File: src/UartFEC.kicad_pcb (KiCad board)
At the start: 2 copper layers, 24 x 27.9 mm, 16 parts, among them J1 B3B-XH-A, P1 105444-0001, U1 FT232RL

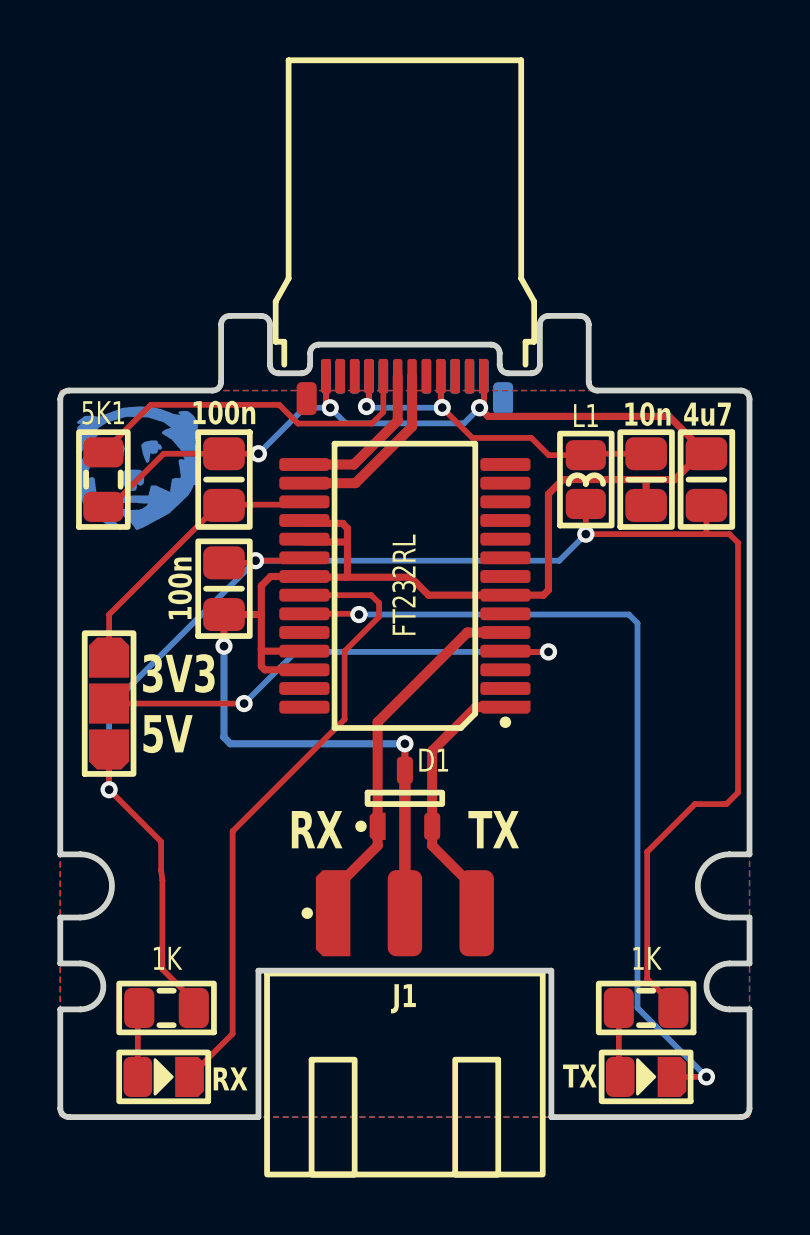
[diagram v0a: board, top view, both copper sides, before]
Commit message: Fixed reset pin (was GND before; now flloating)
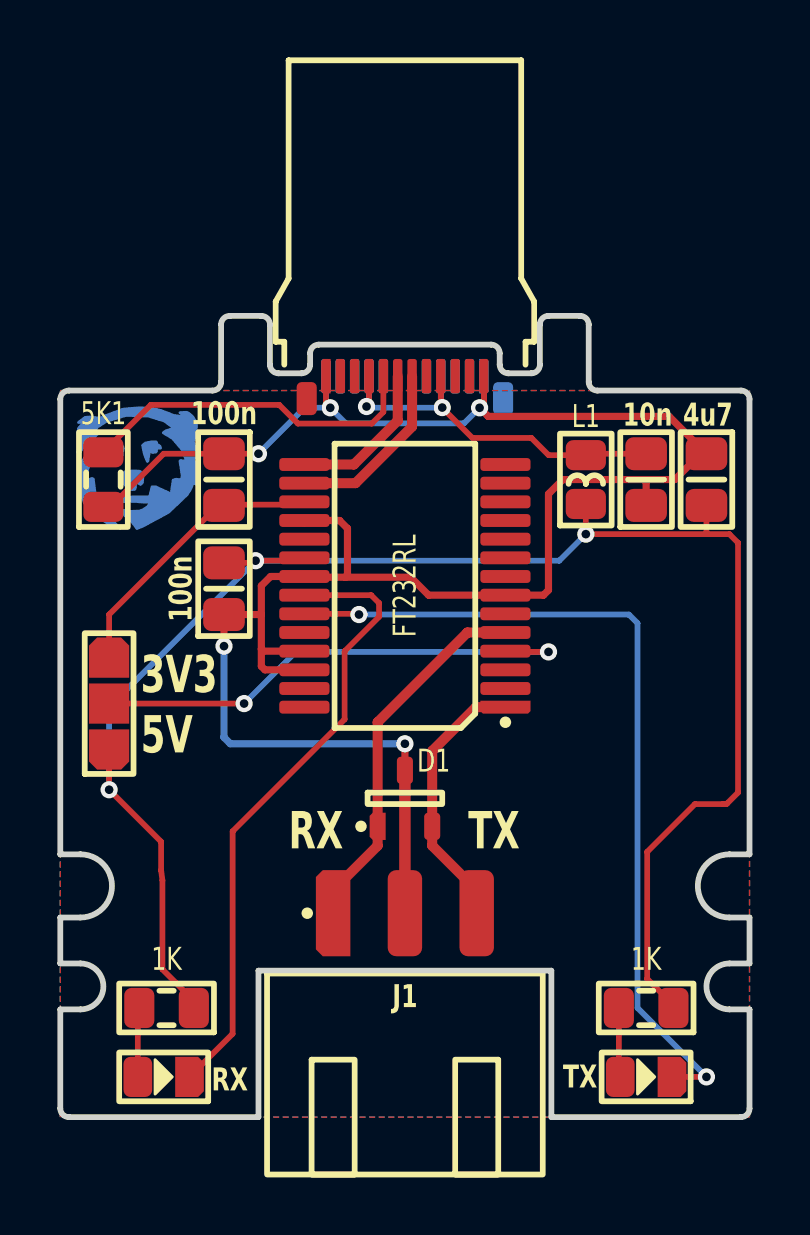
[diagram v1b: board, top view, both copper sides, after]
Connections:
- U1 pad 19: GND -> (no net)
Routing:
- net GND: track 78.3 -> 76.9 mm
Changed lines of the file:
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@@
       (net 7 "GND") (thermal_bridge_angle 45))
     (pad "19" smd roundrect locked (at 3.5 1.625 180) (size 1.75 0.45) (layers "F.Cu" "F.Paste" "F.Mask") (roundrect_rratio 0.25)
-      (net 7 "GND") (thermal_bridge_angle 45))
+      (thermal_bridge_angle 45))
     (pad "20" smd roundrect locked (at 3.5 0.975 180) (size 1.75 0.45) (layers "F.Cu" "F.Paste" "F.Mask") (roundrect_rratio 0.25)
       (net 3 "5V") (thermal_bridge_angle 45))
@@
   (segment (start 41.4 25.7) (end 42.3 24.8) (width 0.25) (layer "F.Cu") (net 7))
   (segment (start 36.825 29.725) (end 32.825 29.725) (width 0.25) (layer "F.Cu") (net 7))
-  (segment (start 29.825 27.225) (end 30 27.4) (width 0.25) (layer "F.Cu") (net 7))
   (segment (start 28.525 29.1) (end 29.925 29.1) (width 0.25) (layer "F.Cu") (net 7))
-  (segment (start 29.925 29.1) (end 30 29.025) (width 0.25) (layer "F.Cu") (net 7))
-  (segment (start 30 27.875) (end 28.5 27.875) (width 0.25) (layer "F.Cu") (net 7))
   (segment (start 25.7 30.4) (end 27 30.4) (width 0.25) (layer "F.Cu") (net 7))
-  (segment (start 30 27.4) (end 30 27.875) (width 0.25) (layer "F.Cu") (net 7))
   (segment (start 26.9 24.8) (end 25.7 24.8) (width 0.2) (layer "F.Cu") (net 7))
-  (segment (start 30 29.025) (end 30 27.875) (width 0.25) (layer "F.Cu") (net 7))
-  (segment (start 28.5 27.225) (end 29.825 27.225) (width 0.25) (layer "F.Cu") (net 7))
   (segment (start 37 29.55) (end 36.825 29.725) (width 0.25) (layer "F.Cu") (net 7))
+  (segment (start 30 27.4) (end 30 29.025) (width 0.25) (layer "F.Cu") (net 7))
   (segment (start 32 40.8) (end 32 35.825) (width 0.4) (layer "F.Cu") (net 7))
   (segment (start 40.325 25.7) (end 41.4 25.7) (width 0.25) (layer "F.Cu") (net 7))
@@
   (segment (start 28.5 31.675) (end 27.075 31.675) (width 0.25) (layer "F.Cu") (net 7))
   (segment (start 41.2 23.5) (end 42.5 24.8) (width 0.25) (layer "F.Cu") (net 7))
+  (segment (start 28.5 27.225) (end 28.6 27.125) (width 0.25) (layer "F.Cu") (net 7))
   (segment (start 32.825 29.725) (end 32.2 29.1) (width 0.25) (layer "F.Cu") (net 7))
   (segment (start 40.325 25.7) (end 40.4 25.775) (width 0.25) (layer "F.Cu") (net 7))
@@
   (segment (start 29.25 23.05) (end 29.4 23.2) (width 0.2) (layer "F.Cu") (net 7))
   (segment (start 40.325 25.7) (end 37.5 25.7) (width 0.25) (layer "F.Cu") (net 7))
+  (segment (start 30 29.025) (end 29.925 29.1) (width 0.25) (layer "F.Cu") (net 7))
   (segment (start 37 26.2) (end 37 29.55) (width 0.25) (layer "F.Cu") (net 7))
+  (segment (start 29.725 27.125) (end 30 27.4) (width 0.25) (layer "F.Cu") (net 7))
   (segment (start 34.75 23.05) (end 34.6 23.2) (width 0.2) (layer "F.Cu") (net 7))
   (segment (start 23.6 24.8) (end 25.7 24.8) (width 0.2) (layer "F.Cu") (net 7))
@@
   (segment (start 27 30.4) (end 27 31.6) (width 0.25) (layer "F.Cu") (net 7))
   (segment (start 37.5 25.7) (end 37 26.2) (width 0.25) (layer "F.Cu") (net 7))
+  (segment (start 28.6 27.125) (end 29.725 27.125) (width 0.25) (layer "F.Cu") (net 7))
   (segment (start 21.75 26.65) (end 23.6 24.8) (width 0.2) (layer "F.Cu") (net 7))
   (segment (start 32 35.825) (end 32 34.9) (width 0.25) (layer "F.Cu") (net 7))

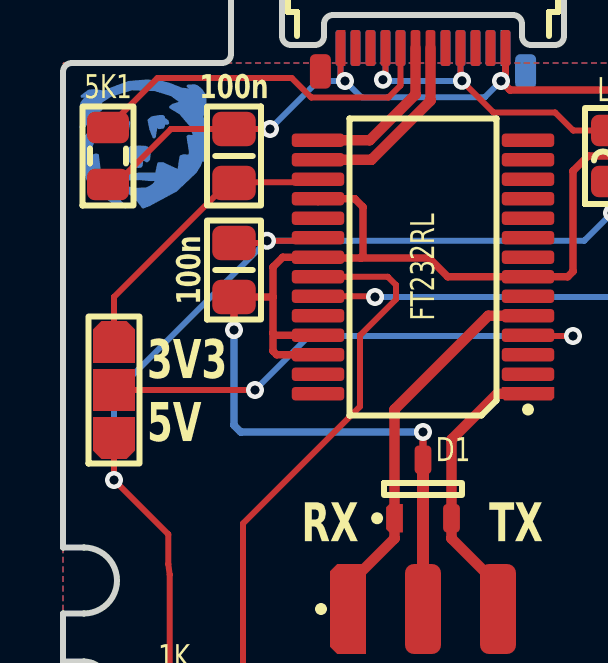
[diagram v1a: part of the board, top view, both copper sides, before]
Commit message: Updated jumper and JST edge connector footprint
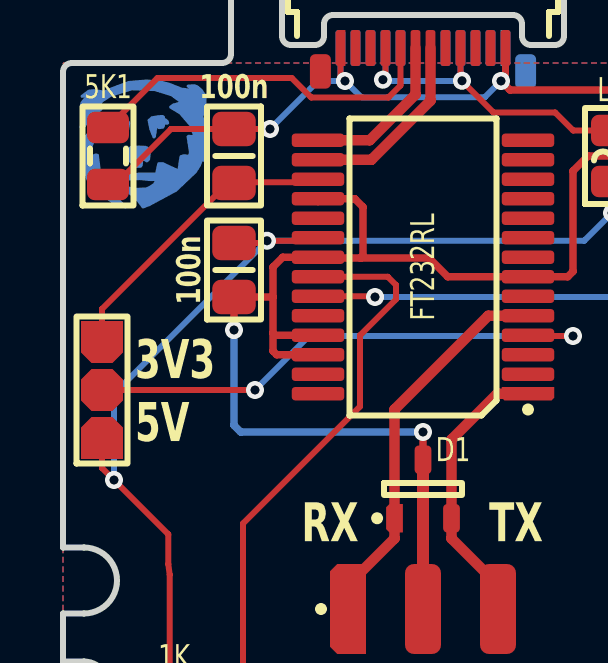
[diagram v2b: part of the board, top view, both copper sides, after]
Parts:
- J1: footprint Medo64:J JST XH Sideway [UART] (3w) -> Medo64:J JST XH Edge [UART] (3w)
- moved JP1 0.40 mm to (21.3, 33.5)
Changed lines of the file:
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@@
     )
   )
-  (footprint "Medo64:J JST XH Sideway [UART] (3w)" (layer "F.Cu")
+  (footprint "Medo64:J JST XH Edge [UART] (3w)" (layer "F.Cu")
     (at 32 40.8)
     (descr "JST B3B-XH-A [455-B3B-XH-A-ND]")
@@
         (effects (font (size 0.13 0.07) (thickness 0.01) bold))
     )
+    (fp_text user "TX" (at 2.5 -1.65) (layer "Cmts.User" knockout)
+        (effects (font (size 0.13 0.07) (thickness 0.01) bold))
+    )
     (fp_text user "GND" (at 0 -1.65) (layer "Cmts.User" knockout)
-        (effects (font (size 0.13 0.07) (thickness 0.01) bold))
-    )
-    (fp_text user "TX" (at 2.5 -1.65) (layer "Cmts.User" knockout)
         (effects (font (size 0.13 0.07) (thickness 0.01) bold))
     )
@@
   )
   (footprint "Medo64:JP Dual (1205)" (layer "F.Cu")
-    (at 21.7 33.5 90)
+    (at 21.3 33.5 90)
     (attr smd)
     (fp_text reference "JP1" (at 0 -1.5 90) (layer "F.SilkS") hide
@@
     (fp_rect (start -2.45 -0.85) (end 2.45 0.85)
       (stroke (width 0.2) (type default)) (fill none) (layer "F.SilkS"))
-    (fp_rect (start -0.9 -0.7) (end -0.7 0.7)
+    (fp_rect (start -0.9 -0.35) (end -0.7 0.35)
       (stroke (width 0) (type solid)) (fill solid) (layer "F.Mask"))
-    (fp_rect (start 0.9 -0.7) (end 0.7 0.7)
+    (fp_rect (start 0.9 -0.35) (end 0.7 0.35)
       (stroke (width 0) (type solid)) (fill solid) (layer "F.Mask"))
     (fp_rect (start -2.55 -0.95) (end 2.55 0.95)
       (stroke (width 0.01) (type dash)) (fill none) (layer "F.CrtYd"))
-    (pad "1" smd roundrect (at -1.6 0 90) (size 1.4 1.4) (layers "F.Cu" "F.Mask") (roundrect_rratio 0)
-      (chamfer_ratio 0.2) (chamfer top_left bottom_left)
+    (pad "1" smd roundrect (at -1.6 0 90) (size 1.4 1.4) (layers "F.Cu" "F.Mask") (roundrect_rratio 0.2)
+      (chamfer_ratio 0.25) (chamfer top_right bottom_right)
       (net 3 "5V") (thermal_bridge_angle 45))
     (pad "2" smd roundrect (at 0 0 90) (size 1.4 1.4) (layers "F.Cu" "F.Mask") (roundrect_rratio 0)
-      (chamfer_ratio 0.2) (chamfer)
+      (chamfer_ratio 0.25) (chamfer top_left top_right bottom_left bottom_right)
       (net 10 "Vio") (thermal_bridge_angle 45))
-    (pad "3" smd roundrect (at 1.6 0 90) (size 1.4 1.4) (layers "F.Cu" "F.Mask") (roundrect_rratio 0)
-      (chamfer_ratio 0.2) (chamfer top_right bottom_right)
+    (pad "3" smd roundrect (at 1.6 0 90) (size 1.4 1.4) (layers "F.Cu" "F.Mask") (roundrect_rratio 0.2)
+      (chamfer_ratio 0.25) (chamfer top_left bottom_left)
       (net 9 "3V3") (thermal_bridge_angle 45))
   )
@@
     (effects (font (size 1.3 0.9) (thickness 0.15) bold) (justify bottom))
   )
-  (gr_text "5V" (at 22.8 34.6) (layer "F.SilkS" knockout)
+  (gr_text "5V" (at 22.4 34.6) (layer "F.SilkS" knockout)
     (effects (font (size 1.3 0.9) (thickness 0.15) bold) (justify left))
   )
-  (gr_text "3V3" (at 22.8 32.5) (layer "F.SilkS" knockout)
+  (gr_text "3V3" (at 22.4 32.5) (layer "F.SilkS" knockout)
     (effects (font (size 1.3 0.9) (thickness 0.15) bold) (justify left))
   )
@@
   (segment (start 26.725 28.6) (end 26.8 28.525) (width 0.2) (layer "F.Cu") (net 3))
   (segment (start 43.208226 36.9881) (end 43.08487 37) (width 0.2) (layer "F.Cu") (net 3))
-  (segment (start 21.7 36.5) (end 21.7 35.1) (width 0.2) (layer "F.Cu") (net 3))
+  (segment (start 21.7 36.5) (end 21.3 36.1) (width 0.2) (layer "F.Cu") (net 3))
   (segment (start 40.436628 43.086628) (end 41.4 44.05) (width 0.2) (layer "F.Cu") (net 3))
   (segment (start 23.556148 42.756148) (end 24.65 43.85) (width 0.2) (layer "F.Cu") (net 3))
@@
   (segment (start 23.510568 39.302643) (end 23.556148 39.656148) (width 0.2) (layer "F.Cu") (net 3))
   (segment (start 40.436628 38.664475) (end 40.436628 43.086628) (width 0.2) (layer "F.Cu") (net 3))
+  (segment (start 21.3 36.1) (end 21.3 35.1) (width 0.2) (layer "F.Cu") (net 3))
   (segment (start 43.08487 37) (end 42.101103 37) (width 0.2) (layer "F.Cu") (net 3))
   (via (at 26.8 28.525) (size 0.6) (drill 0.3) (layers "F.Cu" "B.Cu") (net 3))
@@
   (segment (start 30.75 23.070102) (end 30.663983 23.156119) (width 0.2) (layer "B.Cu") (net 8))
   (segment (start 30.707864 23.2) (end 30.663983 23.156119) (width 0.2) (layer "B.Cu") (net 8))
-  (segment (start 21.7 31.9) (end 21.7 30.4) (width 0.2) (layer "F.Cu") (net 9))
+  (segment (start 21.3 30.8) (end 25.5 26.6) (width 0.2) (layer "F.Cu") (net 9))
   (segment (start 28.5 26.575) (end 25.875 26.575) (width 0.2) (layer "F.Cu") (net 9))
-  (segment (start 21.7 30.4) (end 25.5 26.6) (width 0.2) (layer "F.Cu") (net 9))
+  (segment (start 21.3 31.9) (end 21.3 30.8) (width 0.2) (layer "F.Cu") (net 9))
   (segment (start 21.7 33.5) (end 26.400012 33.5) (width 0.2) (layer "F.Cu") (net 10))
   (segment (start 35.525 31.7) (end 37 31.7) (width 0.2) (layer "F.Cu") (net 10))
